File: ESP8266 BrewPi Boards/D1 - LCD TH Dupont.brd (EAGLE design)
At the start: 46.9 x 50.6 mm, 10 parts, among them J1 RJ45-8X

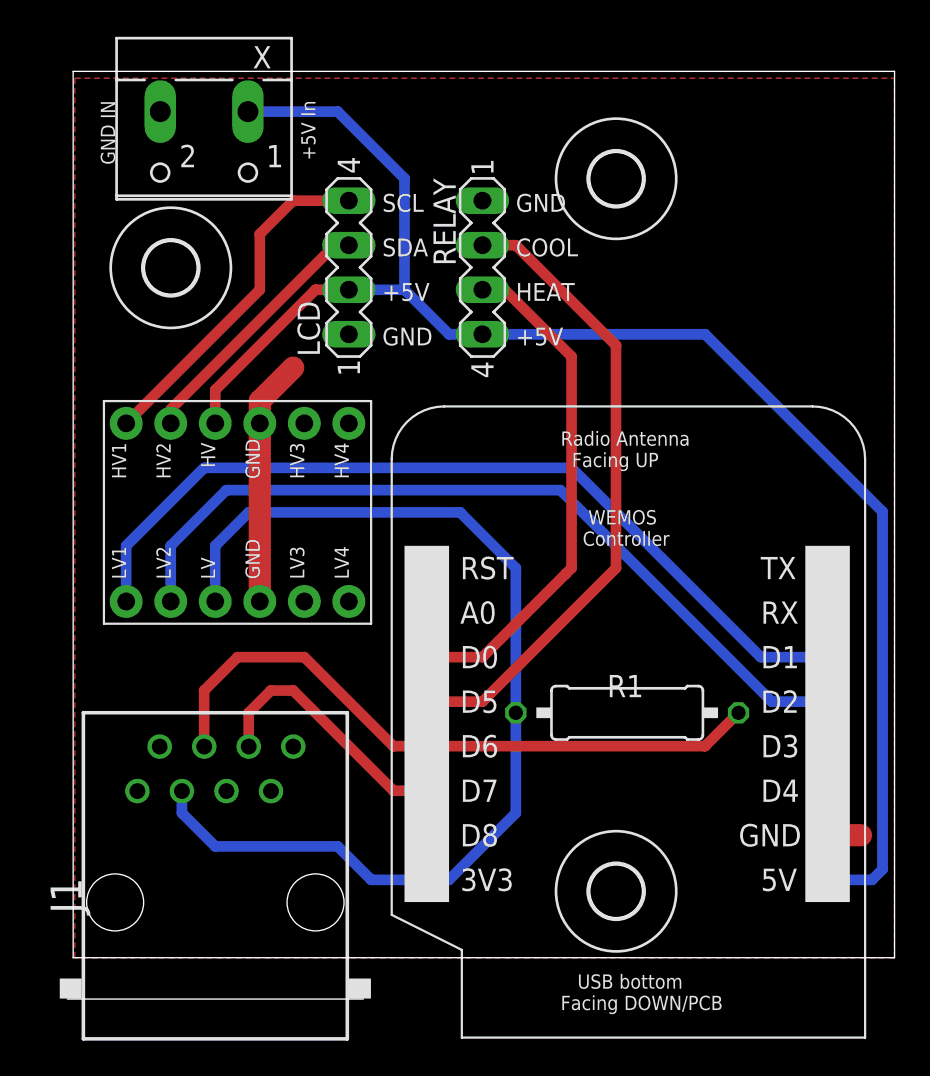
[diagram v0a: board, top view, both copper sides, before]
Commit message: Updating LCD TH Dupont design
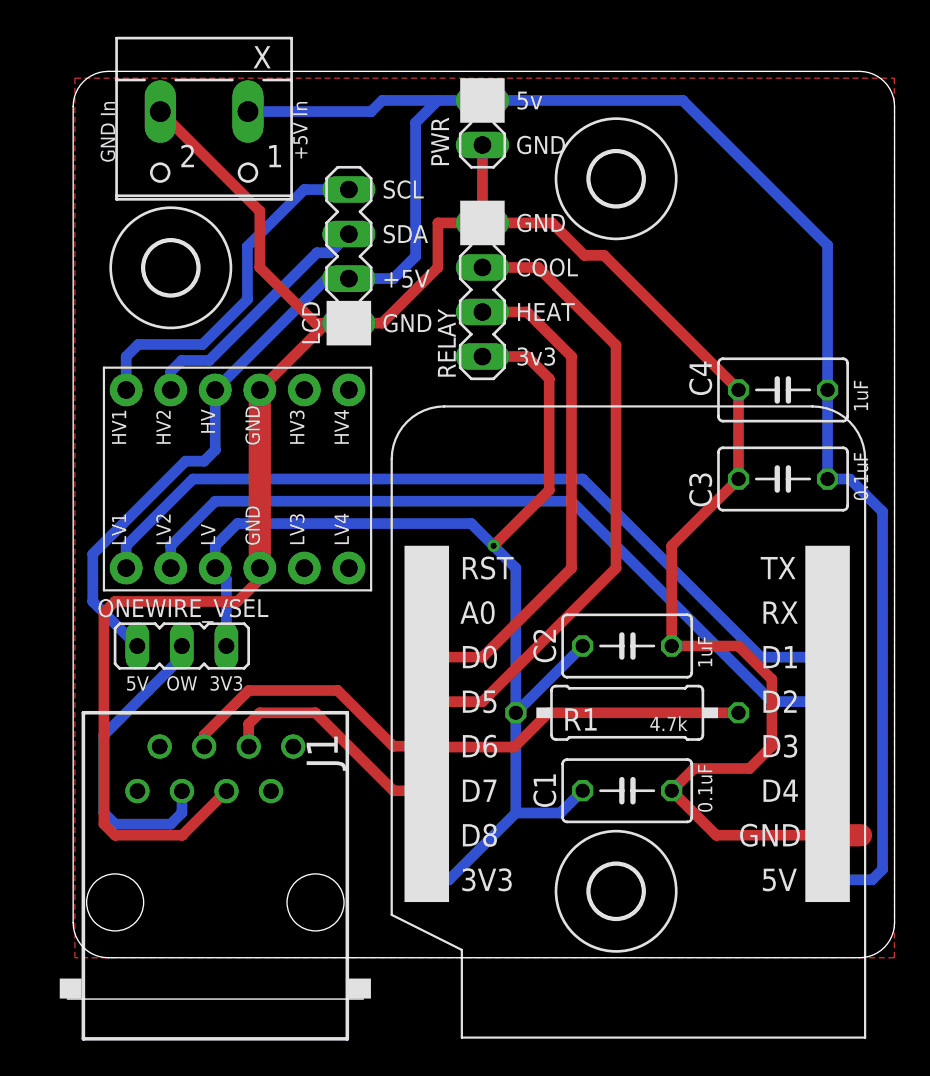
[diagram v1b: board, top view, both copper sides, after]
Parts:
- added C1, C3: 0.1uF, rcl:C050-035X075
- added C2, C4: 1uF, rcl:C050-035X075
- added ONEWIRE_VSEL: (no value), Donnie:JP2-NOLABEL
- added PWR: HDR-2, Donnie:HDR-2_VERT
- LCD, RELAY: value (none) -> HDR-4; device con-lstb:MA04-1 -> Donnie:HDR-4_VERT
- U$1: value WEMOS -> D1_MINI; device 1455413453956-wemos:WEMOS -> 1455413453956-wemos:WEMOS-CLEAN
- moved LCD 3.17 mm to (15.9, 36.2)
- moved RELAY 2.54 mm to (23.5, 41.9)
- moved U$3 1.91 mm to (9.53, 27.3)
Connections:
- new net N$3: J1.3, ONEWIRE_VSEL.2
- net 3V3: now also C1.1, C2.1, ONEWIRE_VSEL.3, RELAY.4; no longer J1.3
- net 5V: now also C3.1, C4.1, ONEWIRE_VSEL.1, PWR.1; no longer RELAY.4
- net GND: now also C1.2, C2.2, C3.2, C4.2, PWR.2
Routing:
- net GND: track 16.0 -> 143.4 mm
- net 5V: track 88.2 -> 120.9 mm
- net N$3: track 0.00 -> 17.6 mm
- net 3V3: track 59.8 -> 70.2 mm, vias 0 -> 1
- net ONEWIRE: track 37.4 -> 34.3 mm
- net N$2: track 47.0 -> 44.5 mm
- net N$1: track 49.5 -> 47.1 mm
- net DOOR: track 15.0 -> 13.6 mm
- net HEAT: track 29.1 -> 28.6 mm
- net COOL: track 36.6 -> 36.1 mm
- net N$4: track 19.8 -> 20.3 mm
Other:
- outline, holes or cut-outs redrawn
- board text added: "0.1uF"
- board text added: "1uF"
- board text added: "3V3"
- board text added: "3v3"
- board text added: "4.7k"
- board text added: "5V"
- board text added: "5v"
- board text added: "BrewPi-ESP8266 D1 Mini TH Dupont - v1.1 @thorrak says hi"
- board text added: "D0 - Heat D1 - I2C SCL D2 - I2C SDA D5 - Cool D6 - OneWire Data D7 - Door"
- board text added: "GND In"
- board text added: "OW"
- board text removed: "BrewPi D1 Mini TH Dupont - v0.2 @thorrak says hi"
- board text removed: "D0 - Heat D1 - I2C SCL D2 - I2C SDA D3 - Buzzer D5 - Cool D6 - OneWire Data D7 - Door"
- board text removed: "GND IN"

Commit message: Updating board designs and adding DirtyPCB Links
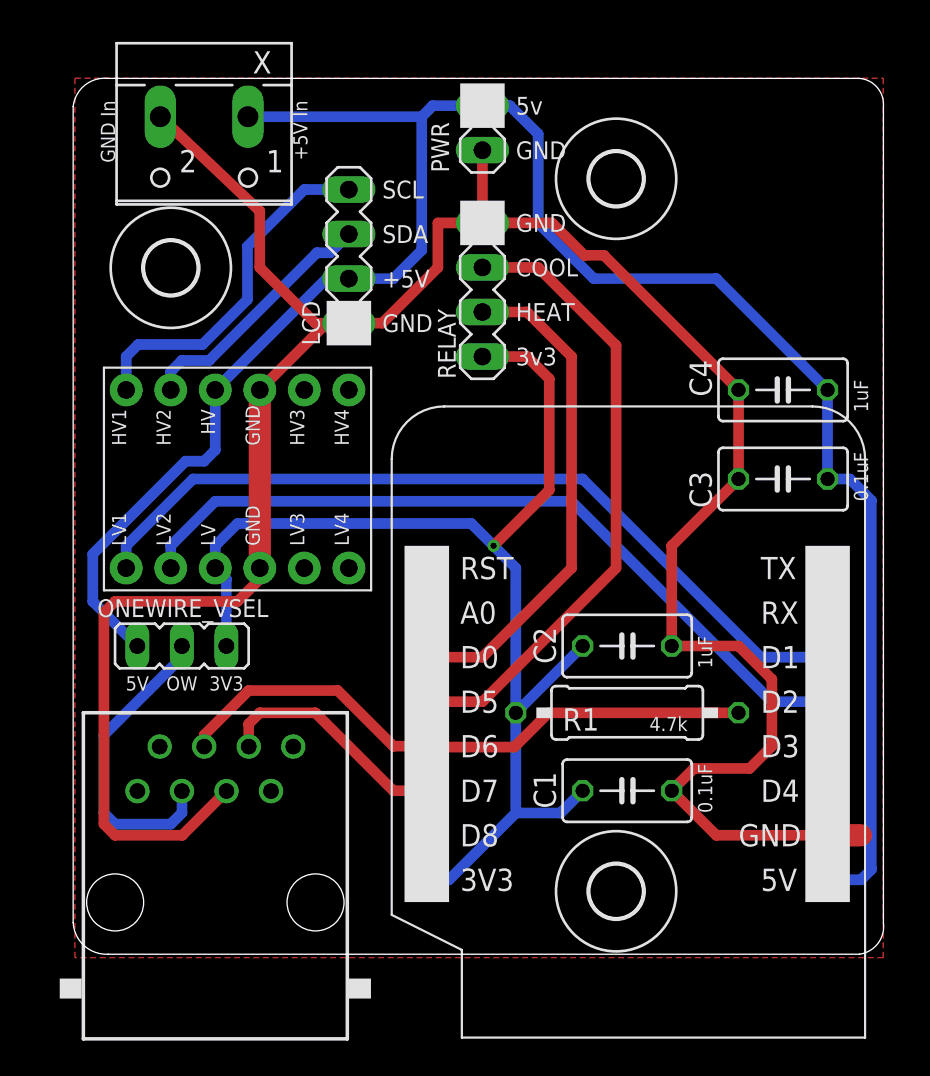
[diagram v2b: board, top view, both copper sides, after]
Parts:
- J1: device con-tycoelectronics:RJ45-NO-SHIELD -> Donnie:RJ45-NS-XDIM
- moved PWR 0.30 mm to (23.5, 48.6)
- moved X 0.29 mm to (7.62, 46.7)
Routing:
- net 5V: track 120.9 -> 116.7 mm
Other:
- board size 46.9 x 50.6 mm -> 46.2 x 50 mm
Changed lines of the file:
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@@
 <plain>
 <wire x1="0.15" y1="48.555" x2="0.15" y2="2" width="0" layer="20"/>
-<wire x1="0.15" y1="2" x2="2.15" y2="0" width="0" layer="20" curve="90"/>
-<wire x1="2.15" y1="0" x2="45" y2="0" width="0" layer="20"/>
-<wire x1="45" y1="0" x2="47" y2="2" width="0" layer="20" curve="90"/>
-<wire x1="47" y1="2" x2="47" y2="48.555" width="0" layer="20"/>
-<wire x1="47" y1="48.555" x2="45" y2="50.555" width="0" layer="20" curve="90"/>
-<wire x1="45" y1="50.555" x2="2.15" y2="50.555" width="0" layer="20"/>
-<wire x1="2.15" y1="50.555" x2="0.15" y2="48.555" width="0" layer="20" curve="90"/>
+<wire x1="0.15" y1="2" x2="2.15" y2="0.2" width="0" layer="20" curve="90"/>
+<wire x1="2.15" y1="0.2" x2="45" y2="0.2" width="0" layer="20"/>
+<wire x1="45" y1="0.2" x2="46.365" y2="2" width="0" layer="20" curve="90"/>
+<wire x1="46.365" y1="2" x2="46.365" y2="48.555" width="0" layer="20"/>
+<wire x1="46.365" y1="48.555" x2="45" y2="50.155" width="0" layer="20" curve="90"/>
+<wire x1="45" y1="50.155" x2="2.15" y2="50.155" width="0" layer="20"/>
+<wire x1="2.15" y1="50.155" x2="0.15" y2="48.555" width="0" layer="20" curve="90"/>
 <text x="25.4" y="36.83" size="1.016" layer="21" font="vector" ratio="12" align="center-left">HEAT</text>
 <text x="25.4" y="39.37" size="1.016" layer="21" font="vector" ratio="12" align="center-left">COOL</text>
@@
 <rectangle x1="41.06595625" y1="48.3268" x2="41.21175" y2="48.33035625" layer="29" grouprefs="LOGO"/>
 <rectangle x1="41.06595625" y1="48.33035625" x2="41.21175" y2="48.3339125" layer="29" grouprefs="LOGO"/>
-<text x="25.4" y="48.895" size="1.016" layer="25" font="vector" ratio="12" align="center-left">5v</text>
-<text x="25.4" y="46.355" size="1.016" layer="25" font="vector" ratio="12" align="center-left">GND</text>
+<text x="25.4" y="48.595" size="1.016" layer="25" font="vector" ratio="12" align="center-left">5v</text>
+<text x="25.4" y="46.055" size="1.016" layer="25" font="vector" ratio="12" align="center-left">GND</text>
 <text x="36.195" y="8.255" size="0.8128" layer="25" font="vector" ratio="12" rot="R90" align="center-left">0.1uF</text>
 <text x="45.085" y="26.035" size="0.8128" layer="25" font="vector" ratio="12" rot="R90" align="center-left">0.1uF</text>
@@
 <elements>
 <element name="U$1" library="1455413453956-wemos" package="WEMOS-CLEAN" value="D1_MINI" x="20.32" y="4.445" smashed="yes"/>
-<element name="X" library="con-wago-500" package="W237-102" value="PWR" x="7.62" y="46.99" smashed="yes" rot="R180">
-<attribute name="MF" value="" x="7.62" y="46.99" size="0.8128" layer="27" rot="R180" display="off"/>
-<attribute name="MPN" value="237-102" x="7.62" y="46.99" size="0.8128" layer="27" rot="R180" display="off"/>
-<attribute name="NAME" x="11.4662" y="51.9938" size="1.27" layer="25" ratio="10" rot="R180"/>
-<attribute name="OC_FARNELL" value="unknown" x="7.62" y="46.99" size="0.8128" layer="27" rot="R180" display="off"/>
-<attribute name="OC_NEWARK" value="70K9898" x="7.62" y="46.99" size="0.8128" layer="27" rot="R180" display="off"/>
-<attribute name="VALUE" x="5.12" y="41.275" size="1.27" layer="27" ratio="10"/>
+<element name="X" library="con-wago-500" package="W237-102" value="PWR" x="7.62" y="46.7" smashed="yes" rot="R180">
+<attribute name="MF" value="" x="7.62" y="46.7" size="0.8128" layer="27" rot="R180" display="off"/>
+<attribute name="MPN" value="237-102" x="7.62" y="46.7" size="0.8128" layer="27" rot="R180" display="off"/>
+<attribute name="NAME" x="11.4662" y="51.7038" size="1.27" layer="25" ratio="10" rot="R180"/>
+<attribute name="OC_FARNELL" value="unknown" x="7.62" y="46.7" size="0.8128" layer="27" rot="R180" display="off"/>
+<attribute name="OC_NEWARK" value="70K9898" x="7.62" y="46.7" size="0.8128" layer="27" rot="R180" display="off"/>
+<attribute name="VALUE" x="5.12" y="40.985" size="1.27" layer="27" ratio="10"/>
 </element>
-<element name="J1" library="con-tycoelectronics" library_urn="urn:adsk.eagle:library:193" package="RJ45-NO-SHIELD" package3d_urn="urn:adsk.eagle:package:10660/1" value="RJ45-8X" x="8.26" y="3.155" smashed="yes">
+<element name="J1" library="Donnie" package="RJ45-NS-XDIM" package3d_urn="urn:adsk.eagle:package:10660/1" value="RJ45-8X" x="8.26" y="3.155" smashed="yes">
 <attribute name="MF" value="" x="8.26" y="3.155" size="1.778" layer="27" display="off"/>
 <attribute name="MPN" value="RJ45-8X" x="8.26" y="3.155" size="1.778" layer="27" display="off"/>
-<attribute name="NAME" x="15.245" y="10.775" size="1.778" layer="25" rot="R90"/>
 <attribute name="OC_FARNELL" value="unknown" x="8.26" y="3.155" size="1.778" layer="27" display="off"/>
 <attribute name="OC_NEWARK" value="16R6101" x="8.26" y="3.155" size="1.778" layer="27" display="off"/>
@@
 <attribute name="VALUE" x="44.196" y="35.814" size="1.27" layer="27" ratio="10" rot="R180"/>
 </element>
-<element name="PWR" library="Donnie" package="HDR-2_VERT" value="HDR-2" x="23.495" y="48.895" smashed="yes" rot="R270">
-<attribute name="NAME" x="21.59" y="45.085" size="1.016" layer="25" font="vector" ratio="12" rot="R270" align="top-right"/>
-<attribute name="VALUE" x="21.59" y="50.165" size="1.27" layer="27" ratio="10" rot="R270" align="top-left"/>
+<element name="PWR" library="Donnie" package="HDR-2_VERT" value="HDR-2" x="23.495" y="48.6" smashed="yes" rot="R270">
+<attribute name="NAME" x="21.59" y="44.79" size="1.016" layer="25" font="vector" ratio="12" rot="R270" align="top-right"/>
+<attribute name="VALUE" x="21.59" y="49.87" size="1.27" layer="27" ratio="10" rot="R270" align="top-left"/>
 </element>
 <element name="ONEWIRE_VSEL" library="Donnie" package="JP2-NOLABEL" value="" x="6.35" y="17.78" smashed="yes">
@@
 <polygon width="0.6096" layer="1" isolate="0.6096">
 <vertex x="0.25" y="50.165"/>
-<vertex x="46.99" y="50.165"/>
-<vertex x="46.99" y="0"/>
+<vertex x="46.355" y="50.165"/>
+<vertex x="46.355" y="0"/>
 <vertex x="0.25" y="0"/>
 </polygon>
@@
 <wire x1="20.955" y1="39.37" x2="20.955" y2="41.91" width="0.6096" layer="1"/>
 <wire x1="20.955" y1="41.91" x2="23.495" y2="41.91" width="0.6096" layer="1"/>
-<wire x1="5.12" y1="48.26" x2="10.795" y2="42.585" width="0.6096" layer="1"/>
+<wire x1="5.12" y1="47.97" x2="10.795" y2="42.585" width="0.6096" layer="1"/>
 <wire x1="10.795" y1="42.585" x2="10.795" y2="39.37" width="0.6096" layer="1"/>
 <wire x1="10.795" y1="39.37" x2="13.97" y2="36.195" width="0.6096" layer="1"/>
@@
 <wire x1="29.31038125" y1="40.0612" x2="30.4238" y2="40.0612" width="0.6096" layer="1"/>
 <wire x1="30.4238" y1="40.0612" x2="38.1" y2="32.385" width="0.6096" layer="1"/>
-<wire x1="23.495" y1="46.355" x2="23.495" y2="41.91" width="0.6096" layer="1"/>
+<wire x1="23.495" y1="46.06" x2="23.495" y2="41.91" width="0.6096" layer="1"/>
 <wire x1="8.895" y1="9.505" x2="6.375" y2="6.985" width="0.6096" layer="1"/>
 <wire x1="6.375" y1="6.985" x2="2.54" y2="6.985" width="0.6096" layer="1"/>
@@
 <contactref element="X" pad="1"/>
 <contactref element="U$3" pad="HV"/>
-<wire x1="46.3142" y1="5.0392" x2="45.72" y2="4.445" width="0.6096" layer="16"/>
-<wire x1="45.72" y1="4.445" x2="43.18" y2="4.445" width="0.6096" layer="16"/>
-<wire x1="46.3142" y1="25.4408" x2="46.3142" y2="5.0392" width="0.6096" layer="16"/>
+<wire x1="45.6792" y1="5.0392" x2="45.085" y2="4.445" width="0.6096" layer="16"/>
+<wire x1="45.085" y1="4.445" x2="43.18" y2="4.445" width="0.6096" layer="16"/>
+<wire x1="45.6792" y1="26.0758" x2="45.6792" y2="5.0392" width="0.6096" layer="16"/>
 <contactref element="LCD" pad="2"/>
 <contactref element="C3" pad="1"/>
@@
 <wire x1="1.27" y1="23.02684375" x2="1.27" y2="20.32" width="0.6096" layer="16"/>
 <wire x1="43.18" y1="27.305" x2="44.45" y2="27.305" width="0.6096" layer="16"/>
-<wire x1="44.45" y1="27.305" x2="46.3142" y2="25.4408" width="0.6096" layer="16"/>
+<wire x1="44.45" y1="27.305" x2="45.6792" y2="26.0758" width="0.6096" layer="16"/>
 <wire x1="43.18" y1="32.385" x2="43.18" y2="27.305" width="0.6096" layer="16"/>
-<wire x1="10.12" y1="48.26" x2="17.145" y2="48.26" width="0.6096" layer="16"/>
-<wire x1="17.145" y1="48.26" x2="17.78" y2="48.895" width="0.6096" layer="16"/>
-<wire x1="17.78" y1="48.895" x2="20.955" y2="48.895" width="0.6096" layer="16"/>
-<wire x1="23.495" y1="48.895" x2="34.925" y2="48.895" width="0.6096" layer="16"/>
-<wire x1="34.925" y1="48.895" x2="43.18" y2="40.64" width="0.6096" layer="16"/>
-<wire x1="43.18" y1="40.64" x2="43.18" y2="32.385" width="0.6096" layer="16"/>
 <contactref element="ONEWIRE_VSEL" pad="1"/>
 <wire x1="3.81" y1="17.78" x2="1.27" y2="20.32" width="0.6096" layer="16"/>
@@
 <wire x1="14.605" y1="38.735" x2="8.255" y2="32.385" width="0.6096" layer="16"/>
 <wire x1="15.875" y1="38.735" x2="18.415" y2="38.735" width="0.6096" layer="16"/>
-<wire x1="18.415" y1="38.735" x2="19.685" y2="40.005" width="0.6096" layer="16"/>
-<wire x1="19.685" y1="40.005" x2="19.685" y2="47.625" width="0.6096" layer="16"/>
-<wire x1="19.685" y1="47.625" x2="20.955" y2="48.895" width="0.6096" layer="16"/>
-<wire x1="20.955" y1="48.895" x2="23.495" y2="48.895" width="0.6096" layer="16"/>
+<wire x1="10.12" y1="47.97" x2="20.03" y2="47.97" width="0.6096" layer="16"/>
+<wire x1="20.66" y1="48.6" x2="23.495" y2="48.6" width="0.6096" layer="16"/>
+<wire x1="20.03" y1="47.97" x2="20.66" y2="48.6" width="0.6096" layer="16"/>
+<wire x1="20.03" y1="40.35" x2="20.03" y2="47.97" width="0.6096" layer="16"/>
+<wire x1="18.415" y1="38.735" x2="20.03" y2="40.35" width="0.6096" layer="16"/>
+<wire x1="43.18" y1="32.385" x2="36.83" y2="38.735" width="0.6096" layer="16"/>
+<wire x1="36.83" y1="38.735" x2="29.845" y2="38.735" width="0.6096" layer="16"/>
+<wire x1="29.845" y1="38.735" x2="26.67" y2="41.91" width="0.6096" layer="16"/>
+<wire x1="26.67" y1="41.91" x2="26.67" y2="46.99" width="0.6096" layer="16"/>
+<wire x1="26.67" y1="46.99" x2="25.06" y2="48.6" width="0.6096" layer="16"/>
+<wire x1="25.06" y1="48.6" x2="23.495" y2="48.6" width="0.6096" layer="16"/>
 </signal>
 <signal name="3V3" class="2">
